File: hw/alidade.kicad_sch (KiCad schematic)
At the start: 0 parts

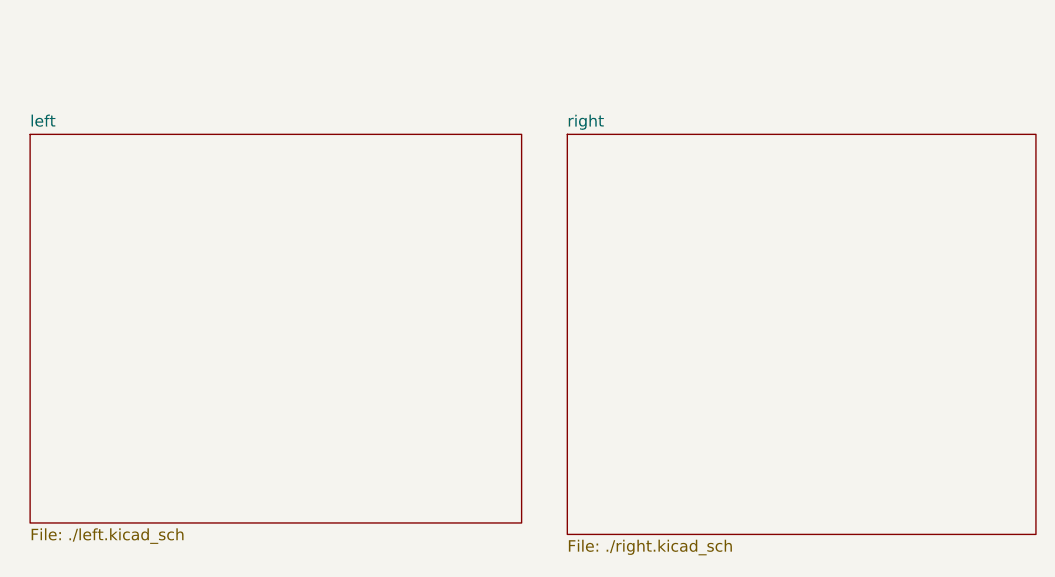
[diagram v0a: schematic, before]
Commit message: clean corne source, setup libraries, place main components
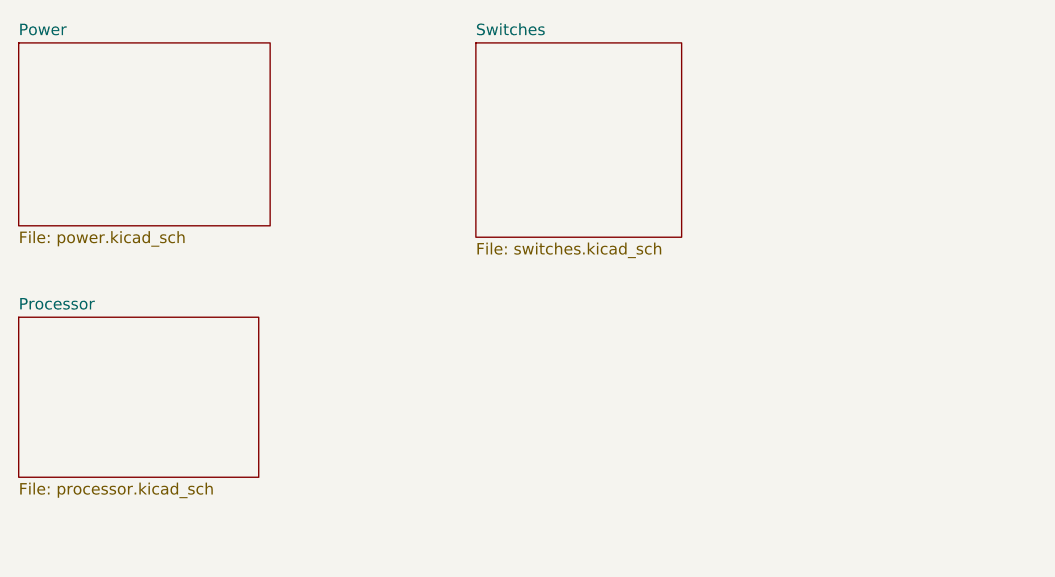
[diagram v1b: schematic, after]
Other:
- removed sheet left
- removed sheet right
- added sheet Power (power.kicad_sch)
- added sheet Processor (processor.kicad_sch)
- added sheet Switches (switches.kicad_sch)
- company: KClark -> Keaton Clark
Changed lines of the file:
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@@
 		(title "Alidade")
 		(rev "0.0.1")
-		(company "KClark")
+		(company "Keaton Clark")
 	)
 	(sheet
-		(at 26.67 38.1)
-		(size 54.61 43.18)
+		(at 25.4 27.94)
+		(size 27.94 20.32)
 		(exclude_from_sim no)
 		(in_bom yes)
@@
 			(color 0 0 0 0.0000)
 		)
-		(property "Sheetname" "left"
-			(at 26.67 37.3884 0)
+		(property "Sheetname" "Power"
+			(at 25.4 27.2284 0)
 			(effects
 				(font
@@
 			)
 		)
-		(property "Sheetfile" "./left.kicad_sch"
-			(at 26.67 81.8646 0)
+		(property "Sheetfile" "power.kicad_sch"
+			(at 25.4 48.8446 0)
 			(effects
 				(font
@@
 			(project "alidade"
 				(path "/4cc5d416-57f5-4147-8183-e03ae6b1198a"
-					(page "2")
+					(page "4")
 				)
 			)
@@
 	)
 	(sheet
-		(at 86.36 38.1)
-		(size 52.07 44.45)
+		(at 76.2 27.94)
+		(size 22.86 21.59)
 		(exclude_from_sim no)
 		(in_bom yes)
@@
 			(color 0 0 0 0.0000)
 		)
-		(property "Sheetname" "right"
-			(at 86.36 37.3884 0)
+		(property "Sheetname" "Switches"
+			(at 76.2 27.2284 0)
 			(effects
 				(font
@@
 			)
 		)
-		(property "Sheetfile" "./right.kicad_sch"
-			(at 86.36 83.1346 0)
+		(property "Sheetfile" "switches.kicad_sch"
+			(at 76.2 50.1146 0)
 			(effects
 				(font
@@
 			(project "alidade"
 				(path "/4cc5d416-57f5-4147-8183-e03ae6b1198a"
-					(page "3")
+					(page "6")
 				)
 			)
+		)
+	)
+	(sheet
+		(at 25.4 58.42)
+		(size 26.67 17.78)
+		(exclude_from_sim no)
+		(in_bom yes)
+		(on_board yes)
+		(dnp no)
+		(fields_autoplaced yes)
+		(stroke
+			(width 0.1524)
+			(type solid)
+		)
+		(fill
+			(color 0 0 0 0.0000)
+		)
+		(property "Sheetname" "Processor"
+			(at 25.4 57.7084 0)
+			(effects
+				(font
+					(size 1.27 1.27)
+				)
+				(justify left bottom)
+			)
+		)
+		(property "Sheetfile" "processor.kicad_sch"
+			(at 25.4 76.7846 0)
+			(effects
+				(font
+					(size 1.27 1.27)
+				)
+				(justify left top)
+			)
+		)
+		(instances
+			(project "alidade"
+				(path "/4cc5d416-57f5-4147-8183-e03ae6b1198a"
+					(page "5")
+				)
+			)

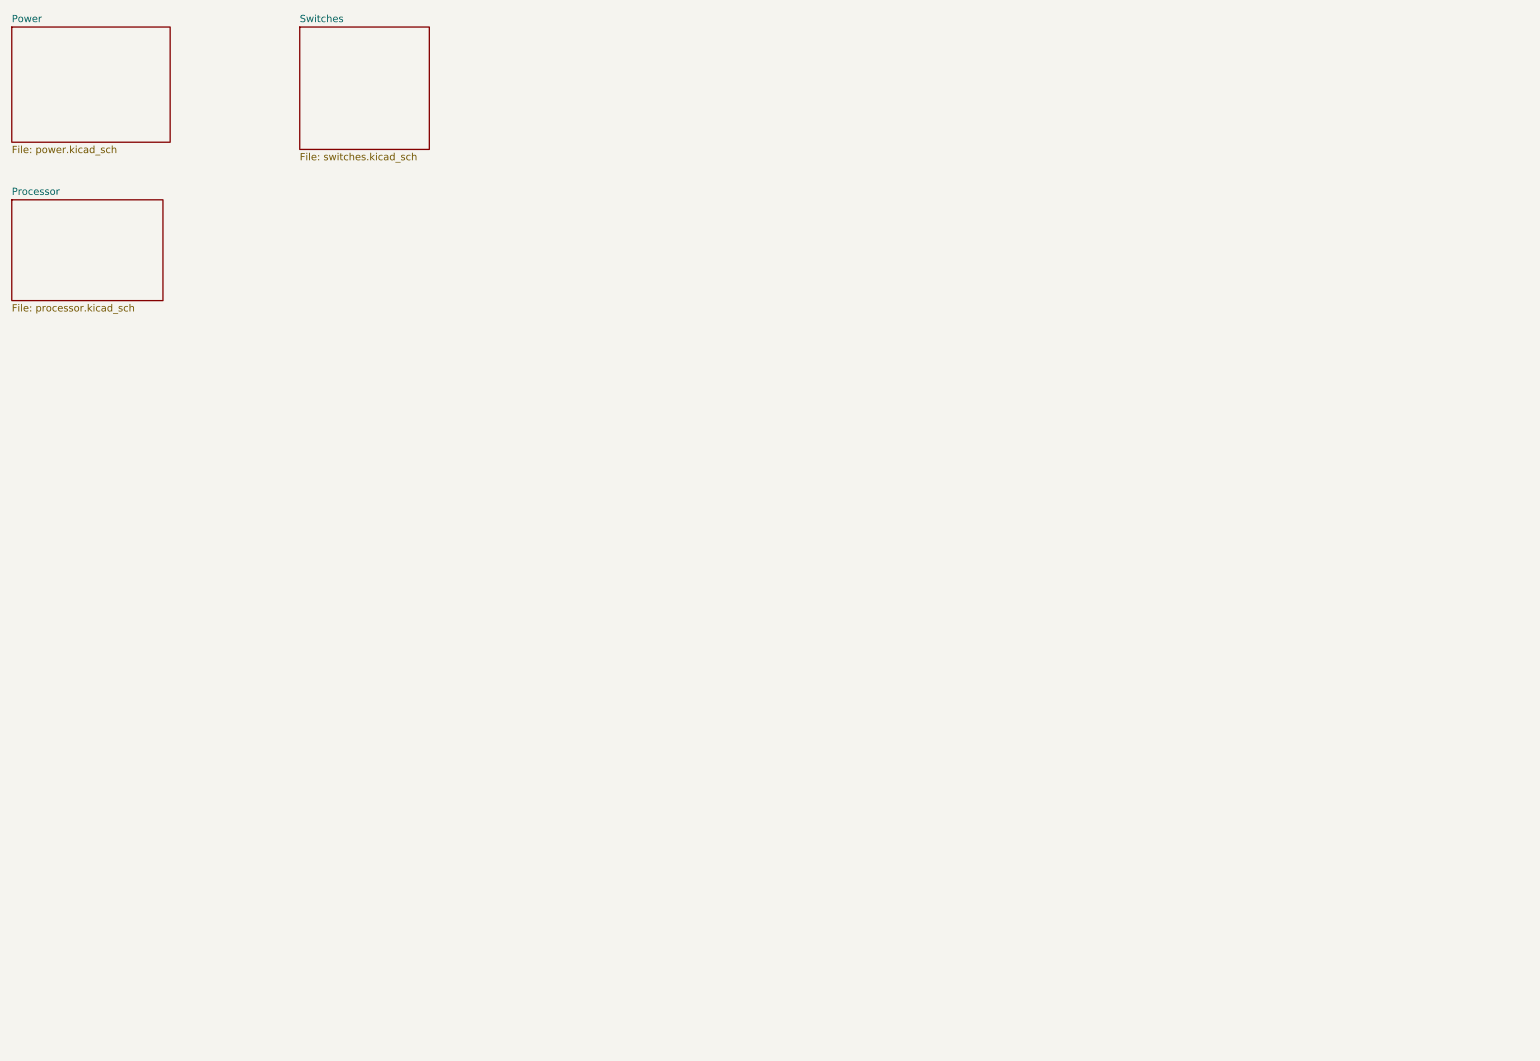
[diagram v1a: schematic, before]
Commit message: Power schematic with npm1100 setup
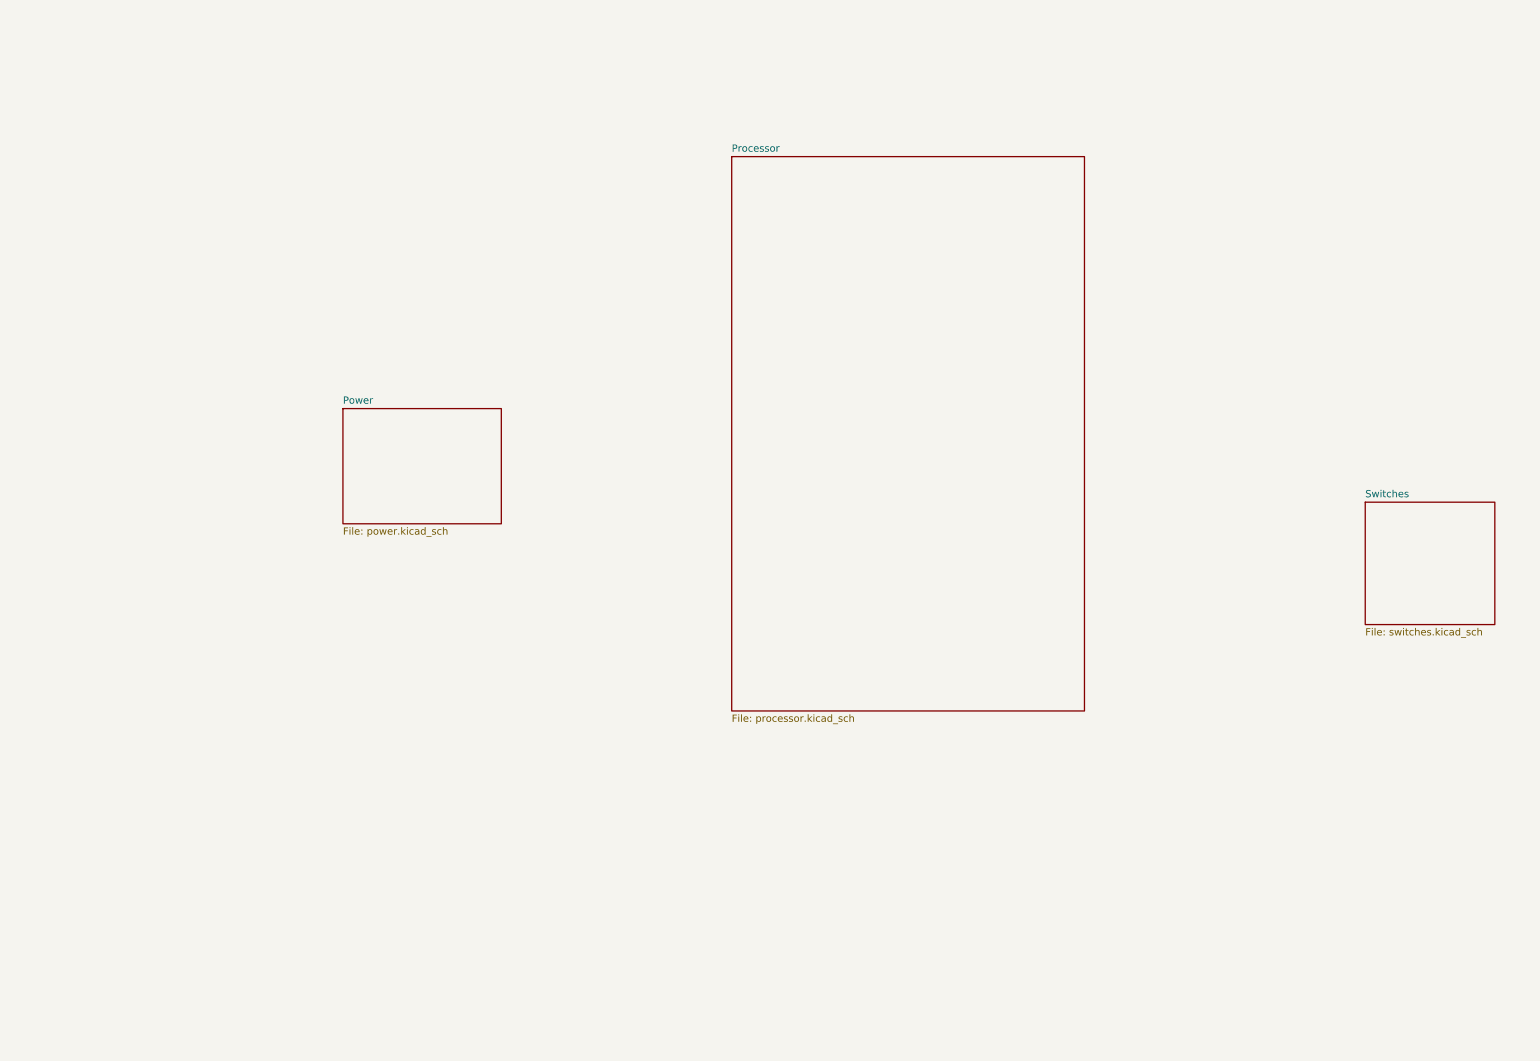
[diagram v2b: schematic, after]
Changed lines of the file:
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@@
 	(generator "eeschema")
 	(generator_version "9.0")
-	(paper "A5")
+	(paper "A3")
 	(title_block
 		(title "Alidade")
@@
 	)
 	(sheet
-		(at 25.4 27.94)
+		(at 83.82 95.25)
 		(size 27.94 20.32)
 		(exclude_from_sim no)
@@
 		)
 		(property "Sheetname" "Power"
-			(at 25.4 27.2284 0)
+			(at 83.82 94.5384 0)
 			(effects
 				(font
@@
 		)
 		(property "Sheetfile" "power.kicad_sch"
-			(at 25.4 48.8446 0)
+			(at 83.82 116.1546 0)
 			(effects
 				(font
@@
 	)
 	(sheet
-		(at 76.2 27.94)
+		(at 264.16 111.76)
 		(size 22.86 21.59)
 		(exclude_from_sim no)
@@
 		)
 		(property "Sheetname" "Switches"
-			(at 76.2 27.2284 0)
+			(at 264.16 111.0484 0)
 			(effects
 				(font
@@
 		)
 		(property "Sheetfile" "switches.kicad_sch"
-			(at 76.2 50.1146 0)
+			(at 264.16 133.9346 0)
 			(effects
 				(font
@@
 	)
 	(sheet
-		(at 25.4 58.42)
-		(size 26.67 17.78)
+		(at 152.4 50.8)
+		(size 62.23 97.79)
 		(exclude_from_sim no)
 		(in_bom yes)
@@
 		)
 		(property "Sheetname" "Processor"
-			(at 25.4 57.7084 0)
+			(at 152.4 50.0884 0)
 			(effects
 				(font
@@
 		)
 		(property "Sheetfile" "processor.kicad_sch"
-			(at 25.4 76.7846 0)
+			(at 152.4 149.1746 0)
 			(effects
 				(font

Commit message: Add sheet pins
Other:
- sheet Power ports: added CHG, ERR, ISET, MODE, SHPACT, rCHG, rERR, rISET, rMODE, rSHPACT; removed none
- sheet Processor ports: added CHG, ERR, ISET, MODE, SHPACT, rCHG, rERR, rISET, rMODE, rSHPACT; removed none

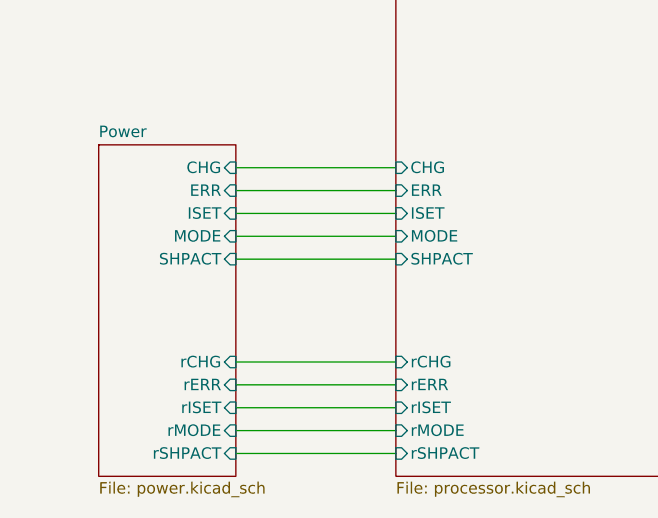
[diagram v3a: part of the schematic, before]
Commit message: Sheet pin directions
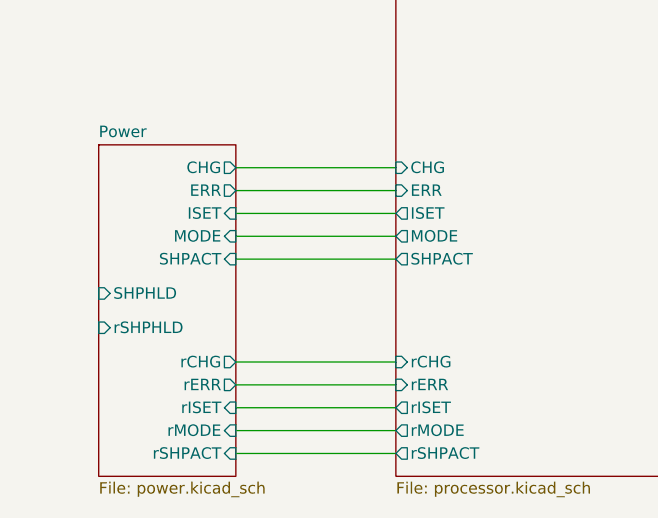
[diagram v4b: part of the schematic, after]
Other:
- sheet Power ports: added SHPHLD, rSHPHLD; removed none
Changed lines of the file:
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@@
-			)
-		)
-		(pin "CHG" input
-			(at 105.41 171.45 0)
-			(effects
-				(font
-					(size 1.27 1.27)
-				)
-				(justify right)
-			)
-		)
-		(pin "ERR" input
-			(at 105.41 173.99 0)
-			(effects
-				(font
-					(size 1.27 1.27)
-				)
-				(justify right)
 			)
 		)
@@
 			)
 		)
-		(pin "rCHG" input
-			(at 105.41 193.04 0)
-			(effects
-				(font
-					(size 1.27 1.27)
-				)
-				(justify right)
-			)
-		)
-		(pin "rERR" input
-			(at 105.41 195.58 0)
-			(effects
-				(font
-					(size 1.27 1.27)
-				)
-				(justify right)
-			)
-		)
 		(pin "rISET" input
 			(at 105.41 198.12 0)
@@
 		(pin "SHPACT" input
 			(at 105.41 181.61 0)
+			(effects
+				(font
+					(size 1.27 1.27)
+				)
+				(justify right)
+			)
+		)
+		(pin "rSHPHLD" input
+			(at 90.17 189.23 180)
+			(effects
+				(font
+					(size 1.27 1.27)
+				)
+				(justify left)
+			)
+		)
+		(pin "SHPHLD" input
+			(at 90.17 185.42 180)
+			(effects
+				(font
+					(size 1.27 1.27)
+				)
+				(justify left)
+			)
+		)
+		(pin "CHG" output
+			(at 105.41 171.45 0)
+			(effects
+				(font
+					(size 1.27 1.27)
+				)
+				(justify right)
+			)
+		)
+		(pin "ERR" output
+			(at 105.41 173.99 0)
+			(effects
+				(font
+					(size 1.27 1.27)
+				)
+				(justify right)
+			)
+		)
+		(pin "rCHG" output
+			(at 105.41 193.04 0)
+			(effects
+				(font
+					(size 1.27 1.27)
+				)
+				(justify right)
+			)
+		)
+		(pin "rERR" output
+			(at 105.41 195.58 0)
 			(effects
 				(font
@@
 			)
 		)
-		(pin "ISET" input
-			(at 123.19 176.53 180)
-			(effects
-				(font
-					(size 1.27 1.27)
-				)
-				(justify left)
-			)
-		)
-		(pin "MODE" input
-			(at 123.19 179.07 180)
-			(effects
-				(font
-					(size 1.27 1.27)
-				)
-				(justify left)
-			)
-		)
 		(pin "rCHG" input
 			(at 123.19 193.04 180)
@@
 			)
 		)
-		(pin "rISET" input
+		(pin "ISET" output
+			(at 123.19 176.53 180)
+			(effects
+				(font
+					(size 1.27 1.27)
+				)
+				(justify left)
+			)
+		)
+		(pin "MODE" output
+			(at 123.19 179.07 180)
+			(effects
+				(font
+					(size 1.27 1.27)
+				)
+				(justify left)
+			)
+		)
+		(pin "SHPACT" output
+			(at 123.19 181.61 180)
+			(effects
+				(font
+					(size 1.27 1.27)
+				)
+				(justify left)
+			)
+		)
+		(pin "rISET" output
 			(at 123.19 198.12 180)
 			(effects
@@
 			)
 		)
-		(pin "rMODE" input
+		(pin "rMODE" output
 			(at 123.19 200.66 180)
 			(effects
@@
 			)
 		)
-		(pin "rSHPACT" input
+		(pin "rSHPACT" output
 			(at 123.19 203.2 180)
 			(effects
 				(font
-					(size 1.27 1.27)
-				)
-				(justify left)
-			)
-		)
-		(pin "SHPACT" input
-			(at 123.19 181.61 180)
-			(effects
-				(font
